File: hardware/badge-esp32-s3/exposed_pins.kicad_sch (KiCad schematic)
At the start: 7 parts, among them CN1 B4B-PH-SM4-TB (LF)(SN), CN3 HDR-TH_2P-P2.54-V-F, U19 FH2.54-09-02PZD, U6 ZX-SH1.0-4PWT

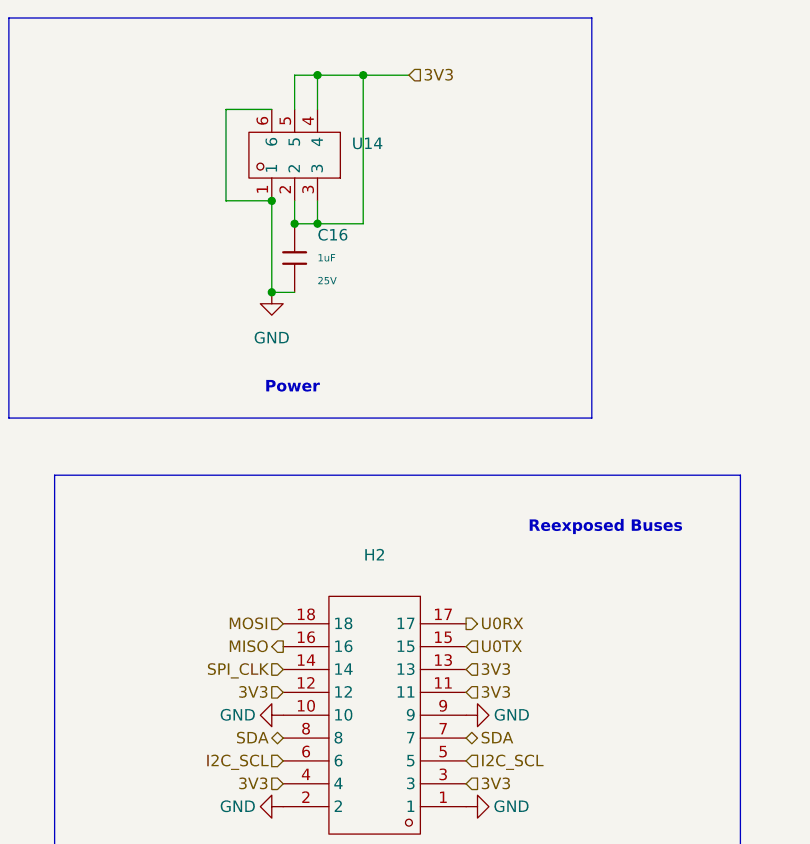
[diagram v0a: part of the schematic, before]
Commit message: Made 5V pins that connect to the +4V line. That is the name of the net coming off of the power switch.
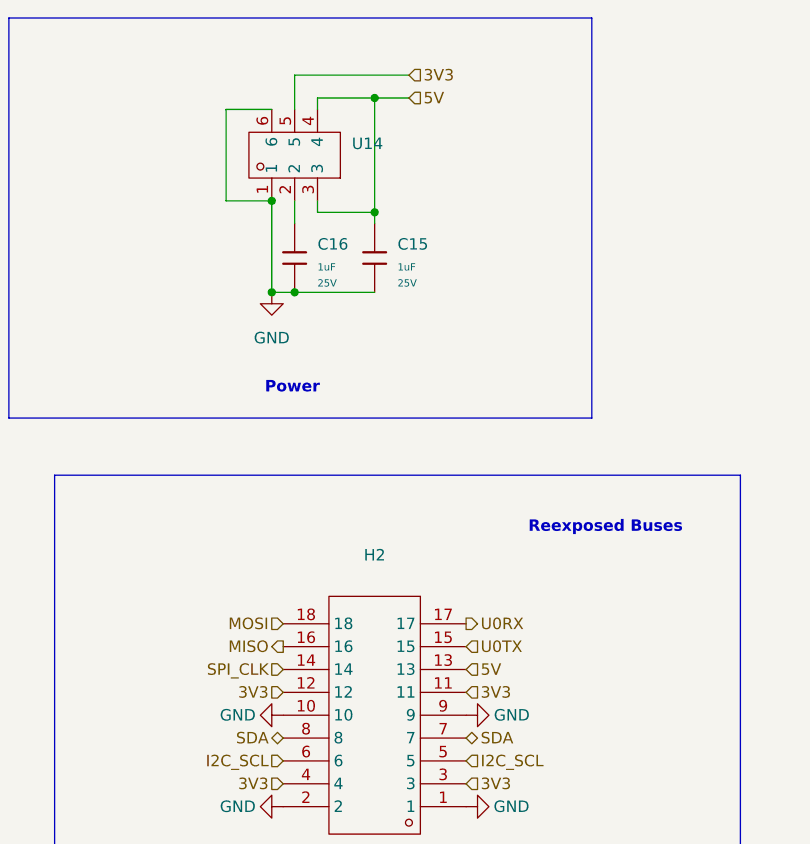
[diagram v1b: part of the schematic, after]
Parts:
- added C15: 1uF, PCM_JLCPCB:C_0402, symbol PCM_JLCPCB-Capacitors:0402,1uF
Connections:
- net 3V3: no longer C16.1, H2.13, U14.2, U14.3, U14.4
- net GND: now also C15.2
- new net: C16.1, U14.2
- new net 5V: C15.1, H2.13, U14.3, U14.4

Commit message: Fixed the wiring for the 3.3V line.
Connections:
- net 3V3: now also C16.1, U14.2
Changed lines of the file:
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@@
+	)
+	(junction
+		(at 140.97 48.26)
+		(diameter 0)
+		(color 0 0 0 0)
 	)
 	(junction
@@
 	)
 	(junction
+		(at 147.32 31.75)
+		(diameter 0)
+		(color 0 0 0 0)
+	)
+	(junction
 		(at 138.43 55.88)
 		(diameter 0)
@@
 	(wire
 		(pts
+			(xy 140.97 48.26) (xy 147.32 48.26)
+		)
+		(stroke
+			(width 0)
+			(type default)
+		)
+	)
+	(wire
+		(pts
 			(xy 153.67 34.29) (xy 149.86 34.29)
 		)
@@
 	(wire
 		(pts
+			(xy 143.51 34.29) (xy 149.86 34.29)
+		)
+		(stroke
+			(width 0)
+			(type default)
+		)
+	)
+	(wire
+		(pts
+			(xy 147.32 31.75) (xy 153.67 31.75)
+		)
+		(stroke
+			(width 0)
+			(type default)
+		)
+	)
+	(wire
+		(pts
 			(xy 140.97 55.88) (xy 149.86 55.88)
 		)
@@
 	(wire
 		(pts
+			(xy 147.32 31.75) (xy 147.32 48.26)
+		)
+		(stroke
+			(width 0)
+			(type default)
+		)
+	)
+	(wire
+		(pts
 			(xy 77.47 129.54) (xy 85.09 129.54)
 		)
@@
 	(wire
 		(pts
-			(xy 149.86 34.29) (xy 143.51 34.29)
-		)
-		(stroke
-			(width 0)
-			(type default)
-		)
-	)
-	(wire
-		(pts
 			(xy 78.74 104.14) (xy 85.09 104.14)
 		)
@@
 	(wire
 		(pts
-			(xy 140.97 31.75) (xy 153.67 31.75)
-		)
-		(stroke
+			(xy 140.97 31.75) (xy 147.32 31.75)
+		)
+		(stroke

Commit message: almost finished
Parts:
- removed H2: ~, lcsc-lib:HDR-TH_18P-P2.54-V-F-R2-C9-S2.54-1, symbol lcsc-lib:DS1023-2*9SF11
- removed U19: FH2.54-09-02PZD, lcsc-lib:HDR-TH_2P-P2.54-V-M-5, symbol lcsc-lib:FH2.54-09-02PZD
- added J3: Conn_02x06_Odd_Even, Connector_PinHeader_2.54mm:PinHeader_2x06_P2.54mm_Vertical, symbol Connector_Generic:Conn_02x06_Odd_Even
- CN3: value HDR-TH_2P-P2.54-V-F -> ~
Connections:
- net IO39 is gone; now on net U0TX: CN3.1
- net IO40 is gone; now on net U0RX: CN3.2
- net 3V3: now also J3.1 (Pin_1), J3.2 (Pin_2)
- net GND: now also J3.11 (Pin_11), J3.5 (Pin_5), J3.6 (Pin_6)
- net I2C_SCL: now also J3.3 (Pin_3)
- net SDA: now also J3.4 (Pin_4)
- net SPI_CLK: now also J3.8 (Pin_8)
- new net SPI_MISO: J3.10 (Pin_10)
- new net SPI_MOSI: J3.12 (Pin_12)
- new net U1RX: J3.9 (Pin_9)
- new net U1TX: J3.7 (Pin_7)
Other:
- note removed: "Also used for minibadge clock Must be 1-10 Hz to follow standard Can be configured to fall out of standard"
- note removed: "GPIO"
- note removed: "Strapping pins (not for ordinary use)"

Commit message: final changes and part updated
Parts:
- removed CN3: ~, lcsc-lib:HDR-TH_2P-P2.54-V-F, symbol lcsc-lib:HX PM2.54-1X2P ZC-Y
- removed U14: ~, lcsc-lib:CONN-TH_HX-PM2.54-2X3P-ZC, symbol lcsc-lib:HX PM2.54-2X3P ZC
- added J11: Conn_02x03_Odd_Even, Connector_PinSocket_2.54mm:PinSocket_2x03_P2.54mm_Vertical, symbol Connector_Generic:Conn_02x03_Odd_Even
- added J14: Conn_01x02_Socket, Connector_PinSocket_2.54mm:PinSocket_1x02_P2.54mm_Vertical, symbol Connector:Conn_01x02_Socket
- J3: footprint Connector_PinHeader_2.54mm:PinHeader_2x06_P2.54mm_Vertical -> Connector_PinSocket_2.54mm:PinSocket_2x06_P2.54mm_Vertical; LCSC (none) -> C5307342
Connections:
- net 3V3: now also J11.3 (Pin_3), J11.4 (Pin_4)
- net 5V: now also J11.5 (Pin_5), J11.6 (Pin_6)
- net GND: now also J3.12 (Pin_12), J11.1 (Pin_1), J11.2 (Pin_2); no longer J3.11 (Pin_11)
- net I2C_SCL: now also J3.4 (Pin_4); no longer J3.3 (Pin_3)
- net SDA: now also J3.3 (Pin_3); no longer J3.4 (Pin_4)
- net SPI_CLK: now also J3.7 (Pin_7); no longer J3.8 (Pin_8)
- net SPI_MISO: now also J3.9 (Pin_9); no longer J3.10 (Pin_10)
- net SPI_MOSI: now also J3.11 (Pin_11); no longer J3.12 (Pin_12)
- net U0RX: now also J14.2 (Pin_2)
- net U0TX: now also J14.1 (Pin_1)
- net U1RX: now also J3.10 (Pin_10); no longer J3.9 (Pin_9)
- net U1TX: now also J3.8 (Pin_8); no longer J3.7 (Pin_7)
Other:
- moved on the sheet: C15, C16

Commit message: finished component alignment
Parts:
- J11, J14, J3: FT Rotation Offset (none) -> -90
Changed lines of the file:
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@@
+			)
+		)
+		(property "FT Rotation Offset" "-90"
+			(at 149.86 46.99 90)
+			(effects
+				(font
+					(size 1.27 1.27)
+				)
+				(hide yes)
 			)
 		)
@@
 			)
 		)
+		(property "FT Rotation Offset" "-90"
+			(at 149.86 101.6 0)
+			(effects
+				(font
+					(size 1.27 1.27)
+				)
+				(hide yes)
+			)
+		)
 		(pin "3"
 		)
@@
 			(at 212.09 102.87 0)
 			(effects
+				(font
+					(size 1.27 1.27)
+				)
+				(hide yes)
+			)
+		)
+		(property "FT Rotation Offset" "-90"
+			(at 212.09 102.87 0)
+			(effects

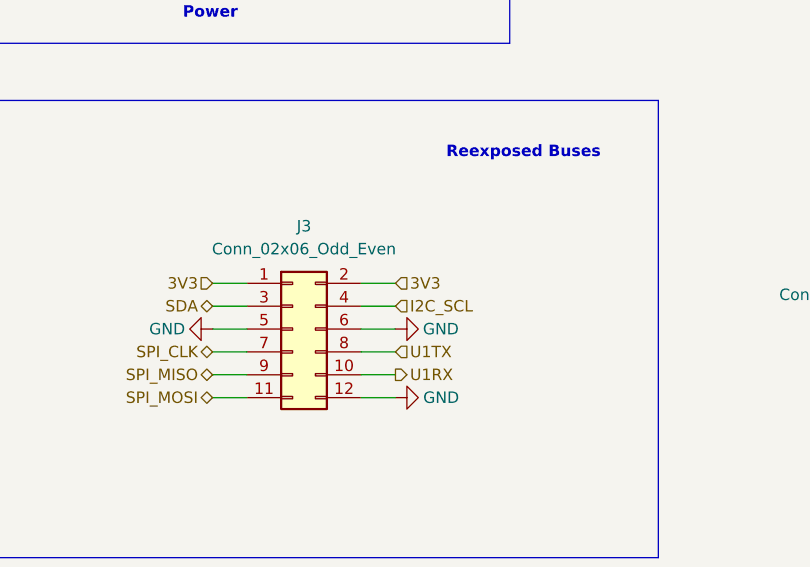
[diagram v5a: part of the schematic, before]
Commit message: changed buck/boost reg and final touchups
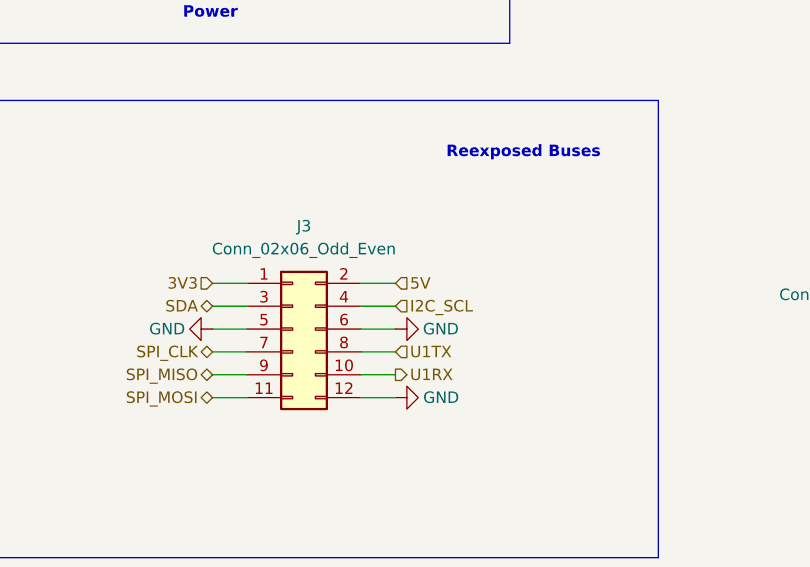
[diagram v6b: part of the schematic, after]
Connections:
- net 3V3: no longer J3.2 (Pin_2)
- net 5V: now also J3.2 (Pin_2)
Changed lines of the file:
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@@
+	(wire
+		(pts
+			(xy 157.48 96.52) (xy 161.29 96.52)
+		)
+		(stroke
+			(width 0)
+			(type default)
+		)
+	)
 	(wire
 		(pts
@@
 	(wire
 		(pts
-			(xy 161.29 96.52) (xy 157.48 96.52)
-		)
-		(stroke
-			(width 0)
-			(type default)
-		)
-	)
-	(wire
-		(pts
 			(xy 152.4 33.02) (xy 152.4 39.37)
 		)
@@
 			(width 0)
 			(type default)
-		)
-	)
-	(hierarchical_label "3V3"
-		(shape input)
-		(at 161.29 96.52 0)
-		(effects
-			(font
-				(size 1.27 1.27)
-			)
-			(justify left)
 		)
 	)
@@
 		(effects
 			(font
+				(size 1.27 1.27)
+			)
+			(justify left)
+		)
+	)
+	(hierarchical_label "5V"
+		(shape input)
+		(at 161.29 96.52 0)
+		(effects
+			(font
